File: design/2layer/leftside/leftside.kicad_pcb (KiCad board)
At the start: 4 copper layers, 142.6 x 96.2 mm, 221 parts, among them IC2 XC9148G50CER-G, IC3 nRF52833-QDAA-R7, IC4 74AHCT125PW,118, IC5 MCP23018T-E_SS, IC6 XC9291B33D1R-G, J1 USB_C_Receptacle_USB2.0_16P, J2 Battery Pos, J3 Battery Neg, J4 OLED_128x32, J6 Conn_01x04, J7 F32Q-1A7H1-11012, U1 BQ27441-G1, U2 BQ24072RGT, U3 USB6B1, U5 PEC11L-4015F-S0015, U6 PEC11L-4015F-S0015, Y1 ECS-320-8-37B2-JTY-TR

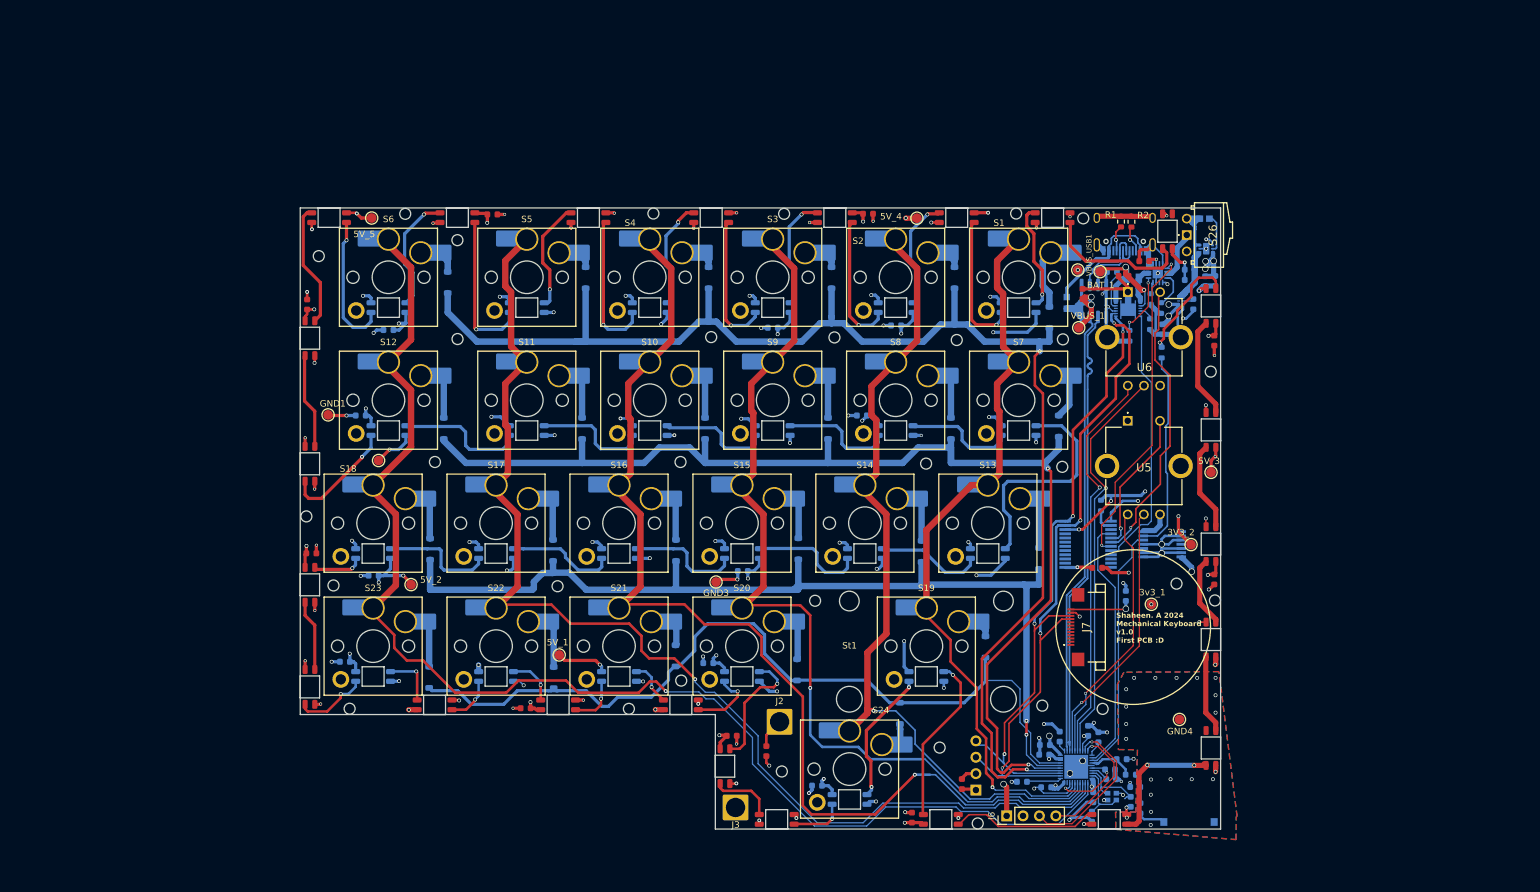
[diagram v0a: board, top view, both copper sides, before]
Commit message: 5v led power plane added
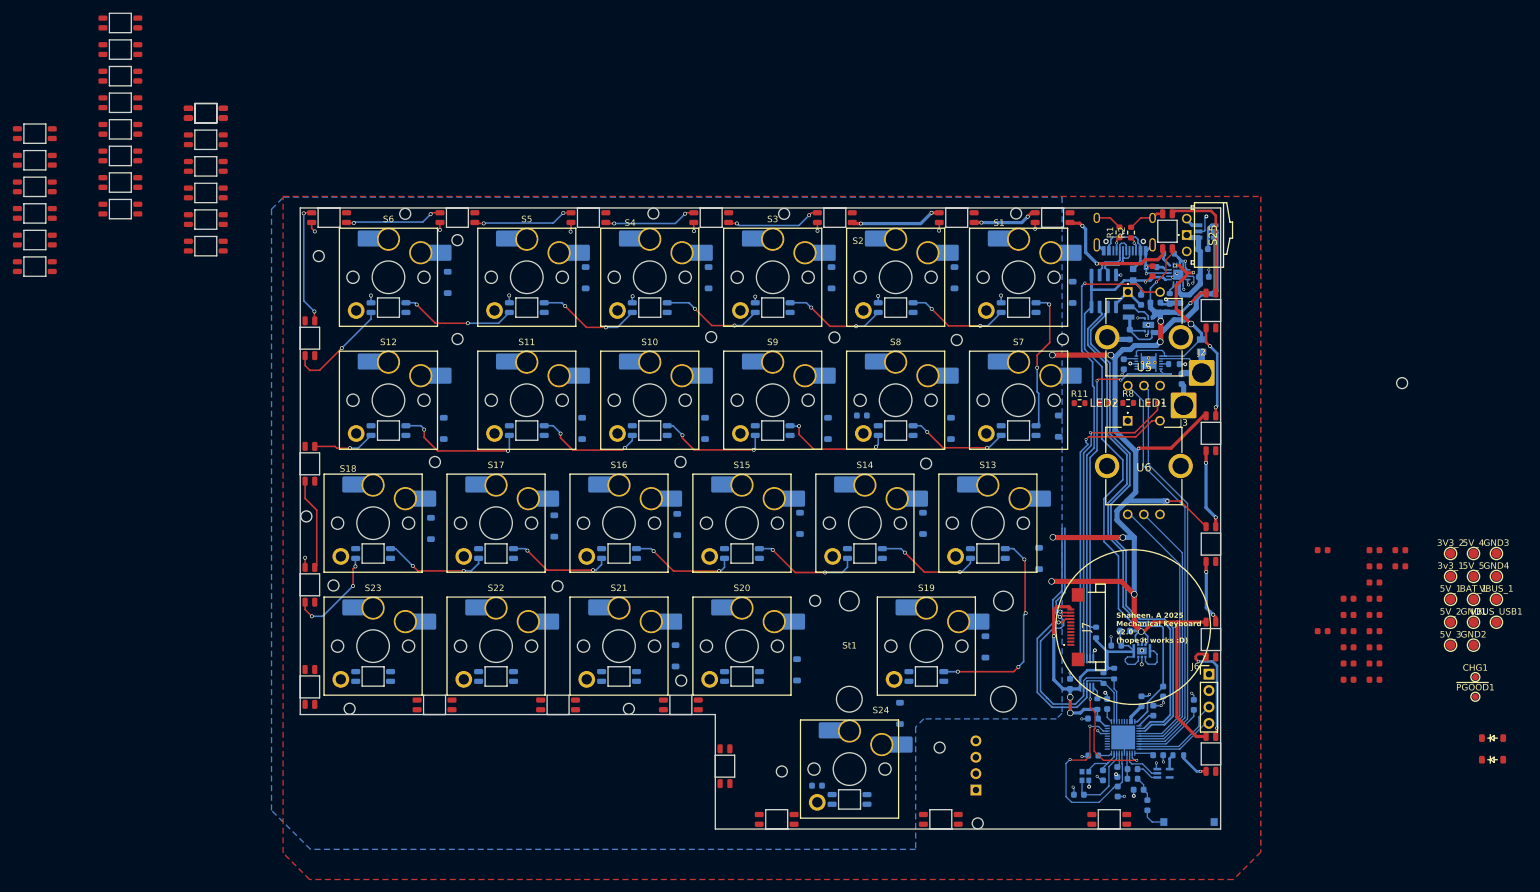
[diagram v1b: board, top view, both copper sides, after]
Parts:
- removed C20: 100nF, ScottoKeebs_Components:Capacitor_0603
- removed IC5: MCP23018T-E_SS, SamacSys_Parts:SOP65P780X200-24N
- removed L5: MCHK1608T1R0MKN, SamacSys_Parts:INDC1608X80N
- removed the REF** at (153.8, 74.5)
- removed the REF** at (142.4, 93.9)
- removed the REF** at (139.4, 17.9)
- removed the REF** at (136.1, 56.4)
- removed the REF** at (159.8, 77.1)
- removed the REF** at (133.0, 93.4)
- added C47: 4.7uF, ScottoKeebs_Components:Capacitor_0603, B.Cu at (145.8, 81.8)
- added C48: 4.7uF, ScottoKeebs_Components:Capacitor_0603, B.Cu at (158.0, 26.9)
- added CHG1: TestPoint, TestPoint:TestPoint_Pad_D1.0mm, F.Cu at (200.1, 88.9)
- added D28: LED_SK6812MINI, ScottoKeebs_Components:LED_SK6812MINI, F.Cu at (-23.1, 4.73)
- added D29: LED_SK6812MINI, ScottoKeebs_Components:LED_SK6812MINI, F.Cu at (-23.1, 8.85)
- added D30: LED_SK6812MINI, ScottoKeebs_Components:LED_SK6812MINI, F.Cu at (-23.1, 13.0)
- added D31: LED_SK6812MINI, ScottoKeebs_Components:LED_SK6812MINI, F.Cu at (-23.1, 17.1)
- added D32: LED_SK6812MINI, ScottoKeebs_Components:LED_SK6812MINI, F.Cu at (-23.1, 21.2)
- added D33: LED_SK6812MINI, ScottoKeebs_Components:LED_SK6812MINI, F.Cu at (-23.1, 25.3)
- added D34: LED_SK6812MINI, ScottoKeebs_Components:LED_SK6812MINI, F.Cu at (-9.84, -12.4)
- added D35: LED_SK6812MINI, ScottoKeebs_Components:LED_SK6812MINI, F.Cu at (-9.84, -8.30)
- added D36, D48: LED_SK6812MINI, ScottoKeebs_Components:LED_SK6812MINI, F.Cu at (3.40, 1.56)
- added D37: LED_SK6812MINI, ScottoKeebs_Components:LED_SK6812MINI, F.Cu at (-9.84, -4.18)
- added D38: LED_SK6812MINI, ScottoKeebs_Components:LED_SK6812MINI, F.Cu at (3.40, 5.68)
- added D39: LED_SK6812MINI, ScottoKeebs_Components:LED_SK6812MINI, F.Cu at (-9.84, -0.06)
- added D40: LED_SK6812MINI, ScottoKeebs_Components:LED_SK6812MINI, F.Cu at (3.40, 9.80)
- added D41: LED_SK6812MINI, ScottoKeebs_Components:LED_SK6812MINI, F.Cu at (-9.84, 4.06)
- added D42: LED_SK6812MINI, ScottoKeebs_Components:LED_SK6812MINI, F.Cu at (3.40, 13.9)
- added D43: LED_SK6812MINI, ScottoKeebs_Components:LED_SK6812MINI, F.Cu at (-9.84, 8.18)
- added D44: LED_SK6812MINI, ScottoKeebs_Components:LED_SK6812MINI, F.Cu at (3.40, 18.0)
- added D45: LED_SK6812MINI, ScottoKeebs_Components:LED_SK6812MINI, F.Cu at (-9.84, 12.3)
- added D46: LED_SK6812MINI, ScottoKeebs_Components:LED_SK6812MINI, F.Cu at (3.40, 22.2)
- added D47: LED_SK6812MINI, ScottoKeebs_Components:LED_SK6812MINI, F.Cu at (-9.84, 16.4)
- added IC1: XCL240B333FR-G, SamacSys_Parts:XCL103D503CRG, B.Cu at (148.4, 85.2)
- added IC7: SN74AHCT1G125DCKR, SamacSys_Parts:SOT65P210X110-5N, B.Cu at (151.8, 103.8)
- added LED1: White LED KW_EEL, SamacSys_Parts:KWEELP41RUS1U13K6L3X4X5R18, F.Cu at (150.1, 46.5)
- added LED2: White LED KW_EEL, SamacSys_Parts:KWEELP41RUS1U13K6L3X4X5R18, F.Cu at (142.6, 46.5)
- added R11: 270, Resistor_SMD:R_0603_1608Metric, F.Cu at (138.8, 46.5)
- added R12: 10k, Resistor_SMD:R_0603_1608Metric, B.Cu at (141.3, 82.0)
- added R13: 4k7, Resistor_SMD:R_0603_1608Metric, B.Cu at (142.5, 89.1)
- added R14: 4k7, Resistor_SMD:R_0603_1608Metric, B.Cu at (144.1, 88.4)
- added R8: 270, Resistor_SMD:R_0603_1608Metric, F.Cu at (146.3, 46.5)
- added ~{PGOOD}1: TestPoint, TestPoint:TestPoint_Pad_D1.0mm, F.Cu at (200.1, 92.0)
- C10: value 4.7uF -> 100pF
- C13: value 4.7uF -> 10uF
- C17, C24: moved to B.Cu
- C18: value 1uF -> 100nF; moved to B.Cu
- C21, C28, C30, C32, C33, C34, C36, C37, C40, Di22, Di23: moved to F.Cu
- IC4: value 74AHCT125PW,118 -> TCA9537DGSR; footprint SamacSys_Parts:SOP65P640X110-14N -> SamacSys_Parts:SOP50P490X110-10N
- IC6: value XC9291B33D1R-G -> TPS22917LDBVT; footprint SamacSys_Parts:XC9290A07E1RG -> SamacSys_Parts:SOT95P280X145-6N
- J2: value Battery Pos -> Battery+
- J3: value Battery Neg -> Battery-
- L3: value 1uH -> 4.7uH; footprint Inductor_SMD:L_0603_1608Metric -> SamacSys_Parts:1286ASH1R0MP2
- moved GND1 180.4 mm to (199.8, 80.4)
- moved 5V_5 179.5 mm to (199.8, 73.3)
- moved C45 173.6 mm to (188.5, 69.3), turned to 0 degrees
- moved GND2 172.0 mm to (199.8, 84.0)
- moved C43 165.6 mm to (184.5, 86.8)
- moved Di23 165.3 mm to (202.8, 101.7), turned to 0 degrees
- moved 5V_2 161.2 mm to (196.3, 80.4)
- moved C36 160.2 mm to (184.5, 71.8), turned to 0 degrees
- moved C34 158.4 mm to (180.5, 89.3), turned to 0 degrees
- moved C32 156.7 mm to (180.5, 84.3), turned to 0 degrees
- moved C28 151.1 mm to (180.5, 76.8), turned to 0 degrees
- moved C35 146.2 mm to (184.5, 69.3)
- moved Di22 145.8 mm to (202.8, 98.4), turned to 0 degrees
- moved 5V_1 138.4 mm to (196.3, 76.9)
- moved C44 131.6 mm to (184.5, 89.3), turned to 0 degrees
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- renumbered D5 to D1, D41 to D10, D39 to D11, D37 to D12, D35 to D13, D34 to D14, D36 to D15, D38 to D16, D40 to D17, D42 to D18, D44 to D19, D4 to D2, D46 to D20, D27 to D21, D28 to D22, D29 to D23, D30 to D24, D31 to D25, D32 to D26, D20 to D27, D33 to D27, D21 to D27, D22 to D28, D23 to D29, D24 to D30, D25 to D31, D26 to D32, D8 to D33, D12 to D34, D14 to D35, D16 to D36, D18 to D37, D19 to D38, D2 to D4, D1 to D5, D48 to D6, D47 to D7, D45 to D8, D43 to D9, S26 to S25, U6 to U5, U5 to U6
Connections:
- C10 pad 1: Net-(IC2-BAT) -> /OUT
- C10 pad 2: GND -> Net-(IC6-CT)
- C13 pad 1: GND -> 3V3
- C13 pad 2: 3V3 -> GND
- C17 pad 1: /BAT -> /SRP
- C18 pad 1: /BAT -> 3V3
- C25 pad 1: Net-(IC2-BAT) -> GND
- C25 pad 2: GND -> Net-(IC2-BAT)
- D1 pad 2: Net-(D5-DOUT) -> Net-(D1-DOUT)
- D1 pad 4: Net-(D4-DOUT) -> Net-(D1-DIN)
- D10 pad 2: Net-(D41-DOUT) -> Net-(D10-DOUT)
- D10 pad 4: Net-(D40-DOUT) -> Net-(D10-DIN)
- D11 pad 2: Net-(D39-DOUT) -> Net-(D11-DOUT)
- D11 pad 4: Net-(D38-DOUT) -> Net-(D10-DOUT)
- D12 pad 2: Net-(D37-DOUT) (its old number) -> Net-(D12-DOUT)
- D12 pad 4: Net-(D36-DOUT) -> Net-(D11-DOUT)
- D13 pad 2: Net-(D35-DOUT) -> Net-(D13-DOUT)
- D13 pad 4: Net-(D34-DOUT) -> Net-(D12-DOUT)
- D14 pad 2: Net-(D34-DOUT) -> Net-(D14-DOUT)
- D14 pad 4: Net-(D33-DOUT) -> Net-(D13-DOUT)
- D15 pad 2: Net-(D36-DOUT) -> Net-(D15-DOUT)
- D15 pad 4: Net-(D35-DOUT) -> Net-(D14-DOUT)
- D16 pad 2: Net-(D38-DOUT) -> Net-(D16-DOUT)
- D16 pad 4: Net-(D37-DOUT) (its old number) -> Net-(D15-DOUT)
- D17 pad 2: Net-(D40-DOUT) -> Net-(D17-DOUT)
- D17 pad 4: Net-(D39-DOUT) -> Net-(D16-DOUT)
- D18 pad 2: Net-(D42-DOUT) -> Net-(D18-DOUT)
- D18 pad 4: Net-(D41-DOUT) -> Net-(D17-DOUT)
- D19 pad 2: Net-(D44-DOUT) -> Net-(D19-DOUT)
- D19 pad 4: Net-(D43-DOUT) -> Net-(D18-DOUT)
- D2 pad 2: Net-(D4-DOUT) -> Net-(D2-DOUT)
- D2 pad 4: Net-(D3-DOUT) -> Net-(D1-DOUT)
- D20 pad 2: Net-(D46-DOUT) -> Net-(D20-DOUT)
- D20 pad 4: Net-(D45-DOUT) -> Net-(D19-DOUT)
- D21 pad 4: Net-(D26-DOUT) -> Net-(D20-DOUT)
- D26 pad 2: Net-(D32-DOUT) -> Net-(D26-DOUT)
- D27 pad 2: Net-(D20-DOUT) -> Net-(D27-DOUT)
- D27 pad 4: Net-(D19-DOUT) -> Net-(D26-DOUT)
- D27 pad 2: Net-(D33-DOUT) -> Net-(D27-DOUT)
- D27 pad 4: Net-(D32-DOUT) -> Net-(D26-DOUT)
- D27 pad 2: Net-(D21-DOUT) (its old number) -> Net-(D27-DOUT)
- D27 pad 4: Net-(D20-DOUT) -> Net-(D26-DOUT)
- D28 pad 4: Net-(D21-DOUT) (its old number) -> Net-(D27-DOUT)
- D32 pad 2: Net-(D26-DOUT) -> Net-(D32-DOUT)
- D33 pad 2: Net-(D8-DOUT) -> Net-(D33-DOUT)
- D33 pad 4: Net-(D7-DOUT) -> Net-(D32-DOUT)
- D34 pad 2: Net-(D12-DOUT) -> Net-(D34-DOUT)
- D34 pad 4: Net-(D11-DOUT) -> Net-(D33-DOUT)
- D35 pad 2: Net-(D14-DOUT) -> Net-(D35-DOUT)
- D35 pad 4: Net-(D13-DOUT) -> Net-(D34-DOUT)
- D36 pad 2: Net-(D16-DOUT) -> Net-(D36-DOUT)
- D36 pad 4: Net-(D15-DOUT) -> Net-(D35-DOUT)
- D37 pad 4: Net-(D17-DOUT) -> Net-(D36-DOUT)
- D38 pad 2: Net-(D19-DOUT) -> Net-(D38-DOUT)
- D4 pad 2: Net-(D2-DOUT) -> Net-(D4-DOUT)
- D4 pad 4: Net-(D1-DOUT) -> Net-(D3-DOUT)
- D5 pad 2: Net-(D1-DOUT) -> Net-(D5-DOUT)
- D5 pad 4: Net-(D1-DIN) -> Net-(D4-DOUT)
- D6 pad 2: unconnected-(D48-DOUT-Pad2) -> Net-(D6-DOUT)
- D6 pad 4: Net-(D47-DOUT) -> Net-(D5-DOUT)
- D7 pad 2: Net-(D47-DOUT) -> Net-(D7-DOUT)
- D7 pad 4: Net-(D46-DOUT) -> Net-(D6-DOUT)
- D8 pad 2: Net-(D45-DOUT) -> Net-(D8-DOUT)
- D8 pad 4: Net-(D44-DOUT) -> Net-(D7-DOUT)
- D9 pad 2: Net-(D43-DOUT) -> Net-(D10-DIN)
- D9 pad 4: Net-(D42-DOUT) -> Net-(D8-DOUT)
- IC3 pad 14: /CW -> /CCW2
- IC3 pad 15: /CCW -> /CW2
- IC3 pad 16: /CCW2 -> /CCW
- IC3 pad 17: /CW2 -> /CW
- IC3 pad 23: /2A -> /A
- IC4 pad 1: GND -> /NO2
- IC4 pad 10: GND -> 3V3
- IC4 pad 2: GND -> /CHG
- IC4 pad 3: unconnected-(IC4-1Y-Pad3) -> /NO
- IC4 pad 4: GND -> /GPOUT
- IC4 pad 5: /2A -> GND
- IC4 pad 6: Net-(IC4-2Y) -> Net-(IC4-~{RESET})
- IC4 pad 7: GND -> /INTA
- IC4 pad 8: unconnected-(IC4-3Y-Pad8) -> /SCL
- IC4 pad 9: GND -> /SDA
- IC6 pad 1: 3V3 -> /OUT
- IC6 pad 2: unconnected-(IC6-NC-Pad2) -> GND
- IC6 pad 3: Net-(IC2-BAT) -> Net-(IC6-ON)
- IC6 pad 4: Net-(IC2-BAT) -> Net-(IC6-CT)
- IC6 pad 5: Net-(IC6-LX) -> Net-(IC2-BAT)
- IC6 pad 6: GND -> Net-(IC2-BAT)
- J2 pad 1: /BAT -> /SRP
- L3 pad 1: 3V3 -> Net-(IC2-BAT)
- L3 pad 2: Net-(IC6-LX) -> Net-(IC2-LX)
- R10 pad 1: Net-(IC4-2Y) -> Net-(IC7-Y)
- R6 pad 2: /BAT_SRN -> /SRP
- R9 pad 1: Net-(IC5-~{RESET}) -> 3V3
- R9 pad 2: 3V3 -> Net-(IC4-~{RESET})
- S25 pad 2: Net-(IC2-BAT) -> Net-(IC6-ON)
- U1 pad 7: /BAT_SRN -> /BAT
- U1 pad 8: /BAT -> /SRP
- U2 pad 2: /BAT_SRN -> /BAT
- U2 pad 3: /BAT_SRN -> /BAT
- U2 pad 6: /VBUS -> /BAT
- U2 pad 7: unconnected-(U2-~{PGOOD}-Pad7) -> /~{PGOOD}
- U5 pad 2: /NO2 -> /NO
- U5 pad A1: /CCW2 -> /CCW
- U5 pad C1: /CW2 -> /CW
- U5 pad MH2: GND -> unconnected-(U5-PadMH2)
- U6 pad 2: /NO -> /NO2
- U6 pad A1: /CCW -> /CCW2
- U6 pad C1: /CW -> /CW2
- U6 pad MH2: unconnected-(U5-PadMH2) -> GND
- Y1 pad 1: Net-(IC3-XC2) -> Net-(IC3-XC1)
- Y1 pad 3: Net-(IC3-XC1) -> Net-(IC3-XC2)
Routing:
- net /Row 0: track 216.8 -> 0.00 mm, vias 2 -> 0
- net /Column 5: track 204.8 -> 0.00 mm, vias 1 -> 0
- net /Row 1: track 183.3 -> 0.00 mm, vias 2 -> 0
- net /Column 4: track 179.3 -> 0.00 mm, vias 1 -> 0
- net GND: track 271.7 -> 95.6 mm, vias 111 -> 46
- net /Column 3: track 169.4 -> 0.00 mm, vias 1 -> 0
- net /Row 2: track 152.5 -> 0.00 mm, vias 2 -> 0
- net /Column 2: track 143.5 -> 0.00 mm, vias 1 -> 0
- net /Row 3: track 132.1 -> 0.00 mm
- net /Column 1: track 127.2 -> 0.00 mm, vias 1 -> 0
- net /Column 0: track 114.4 -> 0.00 mm, vias 1 -> 0
- net /VBUS: track 31.0 -> 100.4 mm, vias 5 -> 1
- net /SCL: track 105.5 -> 51.2 mm, vias 4 -> 1
- net /NO: track 22.0 -> 71.9 mm
- net /SDA: track 100.6 -> 52.9 mm, vias 4 -> 1
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- added copper zone on B.Cu, net 5V
- removed copper zone on In1.Cu, net /BAT
- removed copper zone on In1.Cu, net /VBUS
- removed copper zone on In1.Cu, net 3V3
- removed copper zone on In1.Cu, net 5V
- removed copper zone on B.Cu, net GND
- removed copper zone on In2.Cu, net GND
- removed copper zone on B.Cu, net Net-(IC3-ANT)
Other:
- copper layers 4 -> 2
- board text added: "Shaheen. A 2025 Mechanical Keyboard v2.0 (hope it works :D)"
- board text removed: "Shaheen. A 2024 Mechanical Keyboard v1.0 First PCB :D"

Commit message: LS two layer complete
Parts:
- removed 5V_2, 5V_3, 5V_5, BAT_1, GND4: TestPoint, TestPoint:TestPoint_Pad_D1.5mm
- removed C40, C46: 100nF, ScottoKeebs_Components:Capacitor_0603
- removed the D28 at (-23.1, 4.73)
- removed the D29 at (-23.1, 8.85)
- removed the D30 at (-23.1, 13.0)
- removed the D31 at (-23.1, 17.1)
- removed the D32 at (-23.1, 21.2)
- removed the D33 at (-23.1, 25.3)
- removed the D34 at (-9.84, -12.4)
- removed the D35 at (-9.84, -8.30)
- removed the D36 at (3.40, 1.56)
- removed the D37 at (-9.84, -4.18)
- removed the D38 at (3.40, 5.68)
- removed the D39 at (-9.84, -0.06)
- removed the D40 at (3.40, 9.80)
- removed the D41 at (-9.84, 4.06)
- removed the D42 at (3.40, 13.9)
- removed the D43 at (-9.84, 8.18)
- removed the D44 at (3.40, 18.0)
- removed the D45 at (-9.84, 12.3)
- removed the D46 at (3.40, 22.2)
- removed the D47 at (-9.84, 16.4)
- removed the D48 at (3.40, 1.56)
- removed the REF** at (123.0, 111.6)
- removed the REF** at (77.1, 89.5)
- removed the REF** at (93.0, 17.2)
- removed the REF** at (100.8, 36.3)
- removed the REF** at (42.4, 21.2)
- removed the REF** at (69.0, 93.9)
- added R15: 22, Resistor_SMD:R_0603_1608Metric, B.Cu at (150.9, 95.0)
- added R16: 22, Resistor_SMD:R_0603_1608Metric, B.Cu at (152.0, 96.0)
- added REF**: M1.6 Hole, CustomLibrary:M1.6 Hole, F.Cu at (159.7, 59.3)
- added REF**: M1.6 Hole, CustomLibrary:M1.6 Hole, F.Cu at (159.7, 76.2)
- C21, C28, C31, C32, C33, C35, C36, C44, Di22, Di23: moved to B.Cu
- C29: moved to F.Cu
- R3: value 3k -> 540
- R4: value 1k8 -> 590
- moved GND2 183.4 mm to (20.1, 47.4)
- moved Di23 165.4 mm to (38.3, 84.5), turned to 90 degrees
- moved 5V_1 157.7 mm to (42.9, 40.2)
- moved C33 156.1 mm to (33.5, 34.3), turned to 180 degrees
- moved C34 154.5 mm to (42.2, 20.3)
- moved C35 151.8 mm to (32.7, 72.5)
- moved Di22 146.1 mm to (57.3, 84.7), turned to 90 degrees
- moved C39 139.5 mm to (45.6, 92.7)
- moved C36 119.0 mm to (67.8, 48.4), turned to 180 degrees
- moved C28 118.1 mm to (62.8, 86.5), turned to 180 degrees
- moved GND1 111.4 mm to (90.0, 98.8)
- moved C38 102.3 mm to (86.8, 107.1)
- moved C30 99.1 mm to (100.8, 20.3)
- moved C21 94.9 mm to (93.9, 35.1), turned to -90 degrees
- moved C32 92.0 mm to (89.2, 73.0), turned to -90 degrees
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- renumbered LED1 to CHG, D27 to D28, D27 to D29, D28 to D30, D29 to D31, D30 to D32, D31 to D33, D32 to D34, D33 to D35, D34 to D36, D35 to D37, D36 to D38, D37 to D39, D38 to D40, D17 to D41, D15 to D42, D13 to D43, D11 to D44, D10 to D45, D9 to D46, D7 to D47, D6 to D48, ~{PGOOD}1 to ~{PGOOD}
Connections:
- D28 pad 2: Net-(D27-DOUT) -> Net-(D28-DOUT)
- D28 pad 4: Net-(D26-DOUT) -> Net-(D27-DOUT)
- D29 pad 2: Net-(D27-DOUT) -> Net-(D29-DOUT)
- D29 pad 4: Net-(D26-DOUT) -> Net-(D28-DOUT)
- D30 pad 4: Net-(D27-DOUT) -> Net-(D29-DOUT)
- D40 pad 2: Net-(D38-DOUT) (its old number) -> Net-(D40-DOUT)
- D41 pad 2: Net-(D17-DOUT) -> Net-(D41-DOUT)
- D41 pad 4: Net-(D16-DOUT) -> Net-(D40-DOUT)
- D42 pad 2: Net-(D15-DOUT) -> Net-(D42-DOUT)
- D42 pad 4: Net-(D14-DOUT) -> Net-(D41-DOUT)
- D43 pad 2: Net-(D13-DOUT) -> Net-(D43-DOUT)
- D43 pad 4: Net-(D12-DOUT) -> Net-(D42-DOUT)
- D44 pad 2: Net-(D11-DOUT) -> Net-(D44-DOUT)
- D44 pad 4: Net-(D10-DOUT) -> Net-(D43-DOUT)
- D45 pad 2: Net-(D10-DOUT) -> Net-(D45-DOUT)
- D45 pad 4: Net-(D10-DIN) -> Net-(D44-DOUT)
- D46 pad 2: Net-(D10-DIN) -> Net-(D46-DOUT)
- D46 pad 4: Net-(D8-DOUT) -> Net-(D45-DOUT)
- D47 pad 2: Net-(D7-DOUT) -> Net-(D47-DOUT)
- D47 pad 4: Net-(D6-DOUT) -> Net-(D46-DOUT)
- D48 pad 2: Net-(D6-DOUT) -> unconnected-(D48-DOUT-Pad2)
- D48 pad 4: Net-(D5-DOUT) -> Net-(D47-DOUT)
- IC3 pad 12: D- -> /D2_N
- IC3 pad 13: D+ -> /D2_P
- IC3 pad 4: /Row 0 -> /Row 3
- IC3 pad 5: /Row 1 -> /Row 2
- IC3 pad 6: /Row 2 -> /Row 1
- IC3 pad 7: /Row 3 -> /Row 0
- U2 pad 5: GND -> /BAT
- U2 pad 6: /BAT -> GND
- U5 pad MH2: unconnected-(U5-PadMH2) -> GND
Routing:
- net /Column 5: track 0.00 -> 223.7 mm, vias 0 -> 10
- net /Row 0: track 0.00 -> 201.0 mm, vias 0 -> 14
- net /Column 4: track 0.00 -> 192.3 mm, vias 0 -> 9
- net /Row 1: track 0.00 -> 183.1 mm, vias 0 -> 14
- net /Column 3: track 0.00 -> 166.9 mm, vias 0 -> 7
- net /Row 2: track 0.00 -> 165.0 mm, vias 0 -> 14
- net /Column 1: track 0.00 -> 159.1 mm, vias 0 -> 7
- net /Column 2: track 0.00 -> 144.5 mm, vias 0 -> 5
- net /Row 3: track 0.00 -> 137.3 mm, vias 0 -> 8
- net /Column 0: track 0.00 -> 127.1 mm, vias 0 -> 5
- net 5V: track 194.7 -> 287.9 mm, vias 21 -> 38
- net 3V3: track 72.4 -> 136.4 mm, vias 3 -> 7
- net /SCL: track 51.2 -> 101.1 mm, vias 1 -> 4
- net /SDA: track 52.9 -> 102.3 mm, vias 1 -> 4
- net GND: track 95.6 -> 141.7 mm, vias 46 -> 79
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
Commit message: place components for RS 2 layer
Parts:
- moved IC7 0.36 mm to (151.9, 103.5)
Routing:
- net GND: track 141.7 -> 140.0 mm
- net 5V: track 287.9 -> 287.4 mm, vias 38 -> 44

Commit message: prepare to add in EVQWGD001
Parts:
- removed C27: 10uF-lowESR, ScottoKeebs_Components:Capacitor_0603
- removed IC2: XC9148G50CER-G, SamacSys_Parts:XC9147_8_USP-6C
- removed L3: 4.7uH, SamacSys_Parts:1286ASH1R0MP2
- added IC5: XCL110A503KR-G, SamacSys_Parts:XCL103D503CRG, B.Cu at (149.1, 34.4)
- added R17: 0, Resistor_SMD:R_0603_1608Metric, B.Cu at (150.9, 90.5)
- C26: value 10uF-lowESR -> 10uF
- C43: moved to B.Cu
- F1: value 600mA -> 6A
- moved C43 18.1 mm to (134.5, 20.3), turned to 0 degrees
- moved C24 1.61 mm to (146.8, 31.0), turned to 180 degrees
- moved C4 1.44 mm to (152.5, 91.6), turned to -90 degrees
- moved C2 1.21 mm to (149.4, 91.0), turned to -90 degrees
- moved C25 0.78 mm to (145.9, 35.5)
- moved C1 0.69 mm to (147.7, 93.3)
- moved R5 0.19 mm to (153.1, 23.5)
- moved C26 0.12 mm to (150.4, 30.9), turned to 180 degrees
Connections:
- C2 pad 2: /VBUS -> Net-(IC3-VBUS)
- C26 pad 1: 5V -> GND
- C26 pad 2: GND -> 5V
- IC3 pad 10: /VBUS -> Net-(IC3-VBUS)
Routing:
- net 5V: track 287.4 -> 300.3 mm, vias 44 -> 43
- net Net-(IC3-VBUS): track 0.00 -> 6.85 mm
- net /VBUS: track 105.4 -> 99.1 mm
- net Net-(IC5-5/Lx): track 0.00 -> 5.80 mm
- net Net-(IC2-LX): track 4.04 -> 0.00 mm
- net GND: track 140.0 -> 138.7 mm, vias 79 -> 80
- net Net-(IC3-DECUSB): track 5.19 -> 6.17 mm
- net Net-(IC5-1/VIN): track 32.0 -> 31.1 mm
- added copper zone on B.Cu, net Net-(IC5-1/VIN)
